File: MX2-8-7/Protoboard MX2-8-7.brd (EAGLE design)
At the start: 64.6 x 71.2 mm, 442 parts, among them J1 DCJ0202

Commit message: Gerb files
Added herb files
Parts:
- moved PAD442 1.27 mm to (55.9, 7.62)
- moved PAD443 1.27 mm to (40.6, 7.62)
- moved PAD444 1.27 mm to (5.08, 7.62)
- moved PAD445 1.27 mm to (53.3, 7.62)
- moved PAD446 1.27 mm to (38.1, 7.62)
- moved PAD447 1.27 mm to (7.62, 7.62)
- moved PAD448 1.27 mm to (50.8, 7.62)
- moved PAD449 1.27 mm to (35.6, 7.62)
- moved PAD450 1.27 mm to (10.2, 7.62)
- moved PAD451 1.27 mm to (48.3, 7.62)
- moved PAD452 1.27 mm to (33.0, 7.62)
- moved PAD453 1.27 mm to (12.7, 7.62)
- moved PAD454 1.27 mm to (45.7, 7.62)
- moved PAD455 1.27 mm to (30.5, 7.62)
- moved PAD456 1.27 mm to (15.2, 7.62)
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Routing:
- net VDD: track 181.4 -> 187.0 mm
- net N$7: track 20.5 -> 22.9 mm
- net N$33: track 20.4 -> 22.8 mm
- net N$30: track 20.4 -> 22.8 mm
- net N$26: track 20.4 -> 22.6 mm
- net N$5: track 20.4 -> 22.6 mm
- net N$29: track 20.6 -> 22.7 mm
- net N$16: track 20.5 -> 22.6 mm
- net N$10: track 20.7 -> 22.7 mm
- net N$20: track 20.3 -> 22.3 mm
- net N$22: track 21.1 -> 22.9 mm
- net N$40: track 21.0 -> 22.7 mm
- net N$37: track 20.4 -> 22.1 mm
- net N$13: track 20.4 -> 22.1 mm
- net N$19: track 21.1 -> 22.7 mm
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- added copper zone on layer 16, net GND

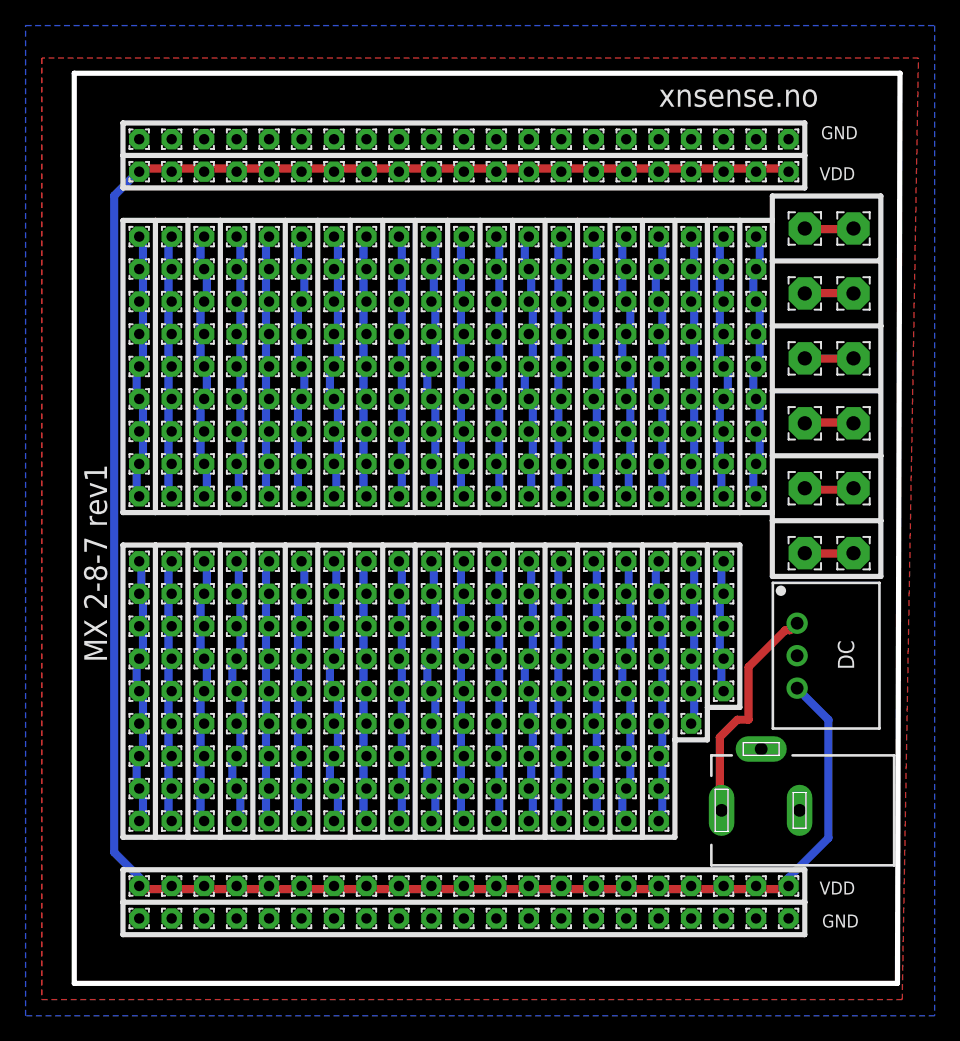
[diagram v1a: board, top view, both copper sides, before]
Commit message: Adjusted Polygon
Adjusted Polygon on all boxes. Changed length on MX-4-7-6 to fit the
box, it was 2mm to long.
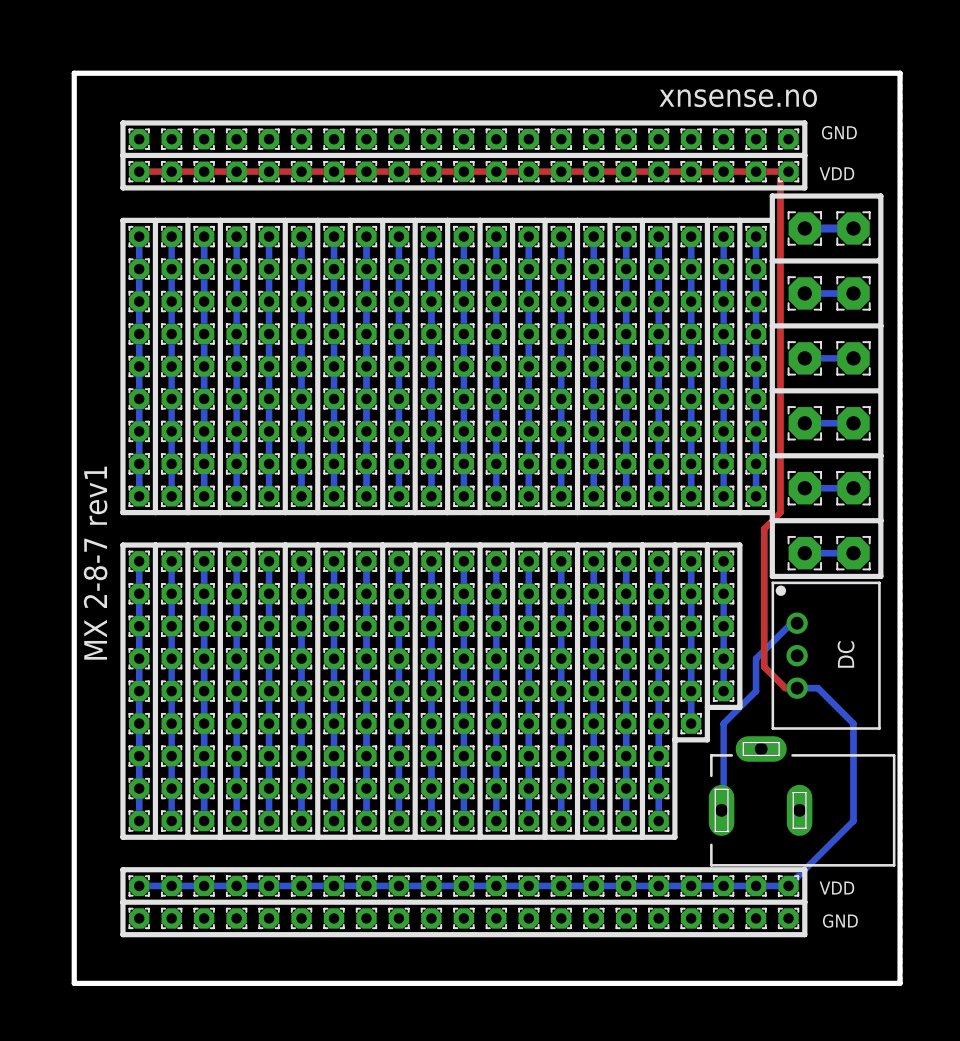
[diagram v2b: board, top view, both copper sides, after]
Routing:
- net VDD: track 187.0 -> 164.8 mm
- net N$15: track 23.0 -> 20.3 mm
- net N$22: track 22.9 -> 20.3 mm
- net N$6: track 22.9 -> 20.3 mm
- net N$7: track 22.9 -> 20.3 mm
- net N$39: track 22.8 -> 20.3 mm
- net N$3: track 22.8 -> 20.3 mm
- net N$33: track 22.8 -> 20.3 mm
- net N$30: track 22.8 -> 20.3 mm
- net N$40: track 22.7 -> 20.3 mm
- net N$29: track 22.7 -> 20.3 mm
- net N$19: track 22.7 -> 20.3 mm
- net N$10: track 22.7 -> 20.3 mm
- net N$12: track 22.7 -> 20.3 mm
- net N$5: track 22.6 -> 20.3 mm
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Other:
- outline, holes or cut-outs redrawn

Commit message: Update to rev2
Updated to Pin headers instead of single wire pads
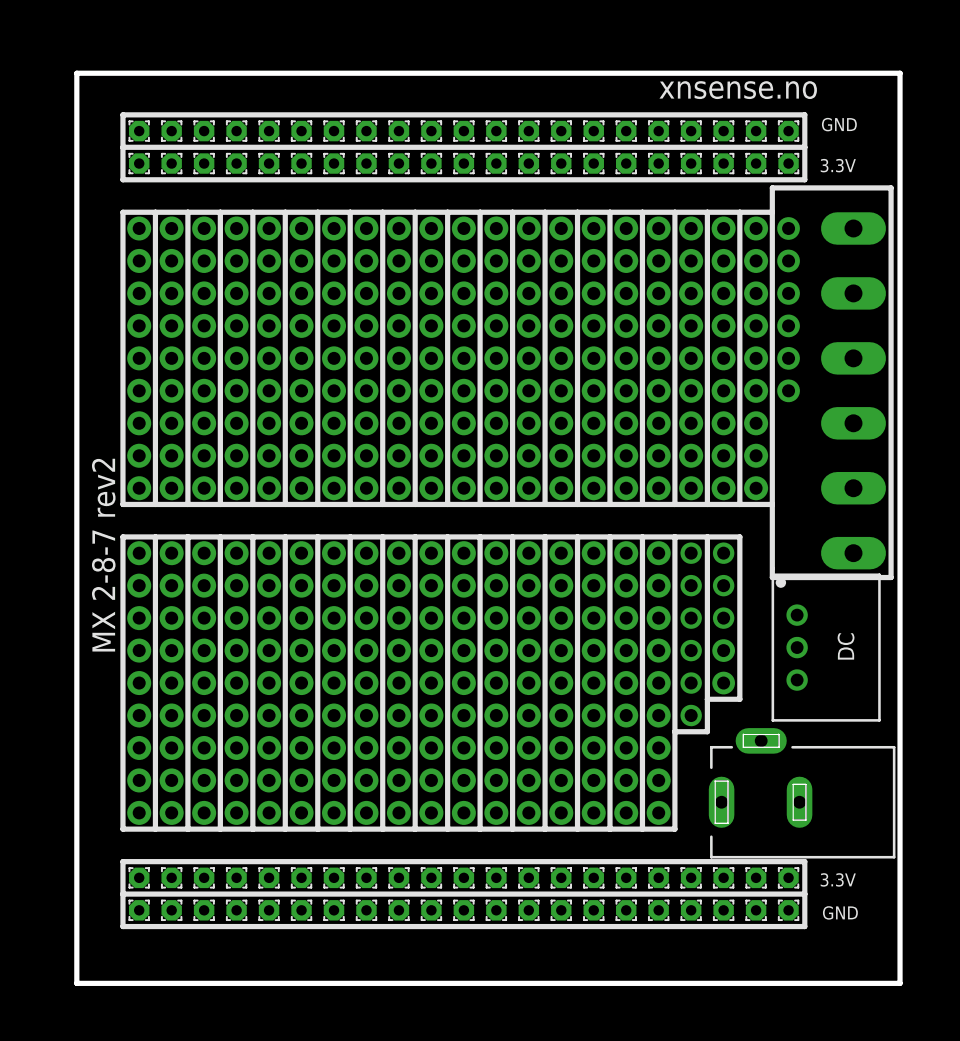
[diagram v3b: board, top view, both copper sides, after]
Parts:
- removed PAD100, PAD101, PAD102, PAD103, PAD104, PAD105, PAD106, PAD107, PAD108, PAD109, PAD110, PAD111, PAD112, PAD113, PAD114, PAD115, PAD116, PAD117, PAD118, PAD119, PAD120, PAD121, PAD122, PAD123, PAD124, PAD125, PAD126, PAD127, PAD128, PAD129, PAD130, PAD131, PAD132, PAD133, PAD134, PAD135, PAD136, PAD137, PAD138, PAD139, PAD140, PAD141, PAD142, PAD143, PAD144, PAD145, PAD146, PAD147, PAD148, PAD149, PAD150, PAD151, PAD152, PAD153, PAD154, PAD155, PAD156, PAD157, PAD158, PAD159, PAD160, PAD161, PAD162, PAD163, PAD164, PAD165, PAD166, PAD167, PAD168, PAD169, PAD170, PAD171, PAD172, PAD173, PAD174, PAD175, PAD176, PAD177, PAD178, PAD179, PAD180, PAD181, PAD182, PAD183, PAD184, PAD185, PAD186, PAD187, PAD188, PAD189, PAD190, PAD191, PAD192, PAD193, PAD194, PAD195, PAD196, PAD197, PAD198, PAD199, PAD20, PAD200, PAD201, PAD202, PAD203, PAD204, PAD205, PAD206, PAD207, PAD208, PAD209, PAD21, PAD210, PAD211, PAD212, PAD213, PAD214, PAD215, PAD216, PAD217, PAD218, PAD219, PAD220, PAD221, PAD222, PAD223, PAD224, PAD225, PAD226, PAD227, PAD228, PAD229, PAD230, PAD231, PAD232, PAD233, PAD234, PAD235, PAD236, PAD237, PAD238, PAD239, PAD240, PAD241, PAD242, PAD243, PAD244, PAD245, PAD246, PAD247, PAD248, PAD249, PAD250, PAD251, PAD252, PAD253, PAD254, PAD255, PAD256, PAD257, PAD258, PAD259, PAD260, PAD261, PAD262, PAD263, PAD264, PAD265, PAD266, PAD267, PAD268, PAD269, PAD270, PAD271, PAD272, PAD273, PAD274, PAD275, PAD276, PAD277, PAD278, PAD279, PAD280, PAD281, PAD282, PAD283, PAD284, PAD285, PAD286, PAD287, PAD288, PAD289, PAD290, PAD291, PAD292, PAD293, PAD294, PAD295, PAD296, PAD297, PAD298, PAD299, PAD300, PAD301, PAD302, PAD303, PAD304, PAD305, PAD306, PAD307, PAD308, PAD309, PAD310, PAD311, PAD312, PAD313, PAD314, PAD315, PAD316, PAD317, PAD318, PAD319, PAD320, PAD321, PAD331, PAD332, PAD333, PAD334, PAD335, PAD336, PAD337, PAD338, PAD339, PAD340, PAD341, PAD342, PAD343, PAD344, PAD345, PAD346, PAD347, PAD348, PAD349, PAD350, PAD351, PAD352, PAD353, PAD354, PAD355, PAD356, PAD357, PAD358, PAD359, PAD360, PAD361, PAD362, PAD363, PAD364, PAD365, PAD366, PAD367, PAD368, PAD369, PAD370, PAD371, PAD372, PAD373, PAD374, PAD375, PAD376, PAD377, PAD378, PAD379, PAD38, PAD380, PAD381, PAD382, PAD383, PAD384, PAD385, PAD386, PAD387, PAD388, PAD389, PAD390, PAD391, PAD392, PAD393, PAD394, PAD395, PAD42, PAD47, PAD48, PAD49, PAD50, PAD51, PAD52, PAD53, PAD54, PAD55, PAD56, PAD57, PAD58, PAD59, PAD60, PAD61, PAD62, PAD63, PAD64, PAD65, PAD66, PAD67, PAD68, PAD69, PAD70, PAD71, PAD72, PAD73, PAD74, PAD75, PAD76, PAD77, PAD78, PAD79, PAD80, PAD81, PAD82, PAD83, PAD84, PAD85, PAD86, PAD87, PAD88, PAD89, PAD90, PAD91, PAD92, PAD93, PAD94, PAD95, PAD96, PAD97, PAD98, PAD99: (no value), wirepad:1,6/0,8
- removed PAD322, PAD323, PAD324, PAD325, PAD326, PAD327, PAD328, PAD329, PAD397, PAD398, PAD399, PAD400: (no value), wirepad:2,54/1,1
- added J10, J11, J12, J13, J14, J15, J16, J17, J18, J19, J2, J20, J21, J22, J23, J24, J25, J26, J27, J28, J29, J3, J30, J31, J32, J33, J34, J35, J36, J37, J38, J4, J5, J6, J7, J8, J9: (no value), SparkFun-Connectors:1X09_NO_SILK
- added JP1, JP10, JP11, JP3, JP4, JP7, JP8, JP9: (no value), adafruit:1X01-CLEANBIG
- added JP12, JP13, JP14, JP15, JP16, JP17: (no value), adafruit:1X1-BIGPOGO
- added JP2, JP5, JP6: (no value), adafruit:1X03-CLEANBIG
- moved PAD15 0.64 mm to (55.9, 64.1)
- moved PAD25 0.64 mm to (5.08, 64.1)
- moved PAD26 0.64 mm to (7.62, 64.1)
- moved PAD27 0.64 mm to (30.5, 64.1)
- moved PAD28 0.64 mm to (25.4, 64.1)
- moved PAD29 0.64 mm to (27.9, 64.1)
- moved PAD30 0.64 mm to (15.2, 64.1)
- moved PAD31 0.64 mm to (12.7, 64.1)
- moved PAD32 0.64 mm to (10.2, 64.1)
- moved PAD33 0.64 mm to (17.8, 64.1)
- moved PAD34 0.64 mm to (33.0, 64.1)
- moved PAD35 0.64 mm to (35.6, 64.1)
- moved PAD36 0.64 mm to (20.3, 64.1)
- moved PAD37 0.64 mm to (43.2, 64.1)
- moved PAD39 0.64 mm to (22.9, 64.1)
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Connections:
- net N$1: now also J2.1, J2.2, J2.3, J2.4, J2.5, J2.6, J2.7, J2.8, J2.9; no longer PAD391.1, PAD392.1, PAD393.1, PAD394.1, PAD395.1
- net N$10: now also J10.1, J10.2, J10.3, J10.4, J10.5, J10.6, J10.7, J10.8, J10.9; no longer PAD106.1, PAD107.1, PAD108.1, PAD109.1, PAD110.1, PAD111.1, PAD112.1, PAD113.1, PAD114.1
- net N$11: now also J11.1, J11.2, J11.3, J11.4, J11.5, J11.6, J11.7, J11.8, J11.9; no longer PAD115.1, PAD116.1, PAD117.1, PAD118.1, PAD119.1, PAD120.1, PAD121.1, PAD122.1, PAD123.1
- net N$12: now also J12.1, J12.2, J12.3, J12.4, J12.5, J12.6, J12.7, J12.8, J12.9; no longer PAD124.1, PAD125.1, PAD126.1, PAD127.1, PAD128.1, PAD129.1, PAD130.1, PAD131.1, PAD132.1
- net N$13: now also J13.1, J13.2, J13.3, J13.4, J13.5, J13.6, J13.7, J13.8, J13.9; no longer PAD133.1, PAD134.1, PAD135.1, PAD136.1, PAD137.1, PAD138.1, PAD139.1, PAD140.1, PAD141.1
- net N$14: now also J14.1, J14.2, J14.3, J14.4, J14.5, J14.6, J14.7, J14.8, J14.9; no longer PAD142.1, PAD143.1, PAD144.1, PAD145.1, PAD146.1, PAD147.1, PAD148.1, PAD149.1, PAD150.1
- net N$15: now also J15.1, J15.2, J15.3, J15.4, J15.5, J15.6, J15.7, J15.8, J15.9; no longer PAD151.1, PAD152.1, PAD153.1, PAD154.1, PAD155.1, PAD156.1, PAD157.1, PAD158.1, PAD159.1
- net N$16: now also J16.1, J16.2, J16.3, J16.4, J16.5, J16.6, J16.7, J16.8, J16.9; no longer PAD160.1, PAD161.1, PAD162.1, PAD163.1, PAD164.1, PAD165.1, PAD166.1, PAD167.1, PAD168.1
- net N$17: now also J17.1, J17.2, J17.3, J17.4, J17.5, J17.6, J17.7, J17.8, J17.9; no longer PAD169.1, PAD170.1, PAD171.1, PAD172.1, PAD173.1, PAD174.1, PAD175.1, PAD176.1, PAD177.1
- net N$18: now also J18.1, J18.2, J18.3, J18.4, J18.5, J18.6, J18.7, J18.8, J18.9; no longer PAD178.1, PAD179.1, PAD180.1, PAD181.1, PAD182.1, PAD183.1, PAD184.1, PAD185.1, PAD186.1
- net N$19: now also J19.1, J19.2, J19.3, J19.4, J19.5, J19.6, J19.7, J19.8, J19.9; no longer PAD187.1, PAD188.1, PAD189.1, PAD190.1, PAD191.1, PAD192.1, PAD193.1, PAD194.1, PAD195.1
- net N$2: now also JP1.1, JP12.P$1; no longer PAD322.1, PAD323.1
- net N$20: now also J20.1, J20.2, J20.3, J20.4, J20.5, J20.6, J20.7, J20.8, J20.9; no longer PAD196.1, PAD197.1, PAD198.1, PAD199.1, PAD200.1, PAD201.1, PAD202.1, PAD203.1, PAD204.1
- net N$21: now also J21.1, J21.2, J21.3, J21.4, J21.5, J21.6, J21.7, J21.8, J21.9; no longer PAD205.1, PAD206.1, PAD207.1, PAD208.1, PAD209.1, PAD210.1, PAD211.1, PAD212.1, PAD213.1
- net N$22: now also J22.1, J22.2, J22.3, J22.4, J22.5, J22.6, J22.7, J22.8, J22.9; no longer PAD214.1, PAD215.1, PAD216.1, PAD217.1, PAD218.1, PAD219.1, PAD220.1, PAD221.1, PAD222.1
- net N$23: now also J23.1, J23.2, J23.3, J23.4, J23.5, J23.6, J23.7, J23.8, J23.9; no longer PAD223.1, PAD224.1, PAD225.1, PAD226.1, PAD227.1, PAD228.1, PAD229.1, PAD230.1, PAD231.1
- net N$24: now also J24.1, J24.2, J24.3, J24.4, J24.5, J24.6, J24.7, J24.8, J24.9; no longer PAD232.1, PAD233.1, PAD234.1, PAD235.1, PAD236.1, PAD237.1, PAD238.1, PAD239.1, PAD240.1
- net N$25: now also J25.1, J25.2, J25.3, J25.4, J25.5, J25.6, J25.7, J25.8, J25.9; no longer PAD241.1, PAD242.1, PAD243.1, PAD244.1, PAD245.1, PAD246.1, PAD247.1, PAD248.1, PAD249.1
- net N$26: now also J26.1, J26.2, J26.3, J26.4, J26.5, J26.6, J26.7, J26.8, J26.9; no longer PAD250.1, PAD251.1, PAD252.1, PAD253.1, PAD254.1, PAD255.1, PAD256.1, PAD257.1, PAD258.1
- net N$27: now also J27.1, J27.2, J27.3, J27.4, J27.5, J27.6, J27.7, J27.8, J27.9; no longer PAD259.1, PAD260.1, PAD261.1, PAD262.1, PAD263.1, PAD264.1, PAD265.1, PAD266.1, PAD267.1
- net N$28: now also J28.1, J28.2, J28.3, J28.4, J28.5, J28.6, J28.7, J28.8, J28.9; no longer PAD268.1, PAD269.1, PAD270.1, PAD271.1, PAD272.1, PAD273.1, PAD274.1, PAD275.1, PAD276.1
- net N$29: now also J29.1, J29.2, J29.3, J29.4, J29.5, J29.6, J29.7, J29.8, J29.9; no longer PAD277.1, PAD278.1, PAD279.1, PAD280.1, PAD281.1, PAD282.1, PAD283.1, PAD284.1, PAD285.1
- net N$3: now also J3.1, J3.2, J3.3, J3.4, J3.5, J3.6, J3.7, J3.8, J3.9; no longer PAD20.1, PAD21.1, PAD38.1, PAD42.1, PAD47.1, PAD48.1, PAD49.1, PAD50.1, PAD51.1
- net N$30: now also J30.1, J30.2, J30.3, J30.4, J30.5, J30.6, J30.7, J30.8, J30.9; no longer PAD286.1, PAD287.1, PAD288.1, PAD289.1, PAD290.1, PAD291.1, PAD292.1, PAD293.1, PAD294.1
- net N$31: now also J31.1, J31.2, J31.3, J31.4, J31.5, J31.6, J31.7, J31.8, J31.9; no longer PAD295.1, PAD296.1, PAD297.1, PAD298.1, PAD299.1, PAD300.1, PAD301.1, PAD302.1, PAD303.1
- net N$32: now also J32.1, J32.2, J32.3, J32.4, J32.5, J32.6, J32.7, J32.8, J32.9; no longer PAD304.1, PAD305.1, PAD306.1, PAD307.1, PAD308.1, PAD309.1, PAD310.1, PAD311.1, PAD312.1
- net N$33: now also J33.1, J33.2, J33.3, J33.4, J33.5, J33.6, J33.7, J33.8, J33.9; no longer PAD313.1, PAD314.1, PAD315.1, PAD316.1, PAD317.1, PAD318.1, PAD319.1, PAD320.1, PAD321.1
- net N$34: now also JP13.P$1, JP7.1; no longer PAD324.1, PAD325.1
- net N$35: now also J34.1, J34.2, J34.3, J34.4, J34.5, J34.6, J34.7, J34.8, J34.9; no longer PAD331.1, PAD332.1, PAD333.1, PAD334.1, PAD335.1, PAD336.1, PAD337.1, PAD338.1, PAD339.1
- net N$36: now also J35.1, J35.2, J35.3, J35.4, J35.5, J35.6, J35.7, J35.8, J35.9; no longer PAD340.1, PAD341.1, PAD342.1, PAD343.1, PAD344.1, PAD345.1, PAD346.1, PAD347.1, PAD348.1
- net N$37: now also J36.1, J36.2, J36.3, J36.4, J36.5, J36.6, J36.7, J36.8, J36.9; no longer PAD349.1, PAD350.1, PAD351.1, PAD352.1, PAD353.1, PAD354.1, PAD355.1, PAD356.1, PAD357.1
- net N$38: now also J37.1, J37.2, J37.3, J37.4, J37.5, J37.6, J37.7, J37.8, J37.9; no longer PAD358.1, PAD359.1, PAD360.1, PAD361.1, PAD362.1, PAD363.1, PAD364.1, PAD365.1, PAD366.1
- net N$39: now also J38.1, J38.2, J38.3, J38.4, J38.5, J38.6, J38.7, J38.8, J38.9; no longer PAD367.1, PAD368.1, PAD369.1, PAD370.1, PAD371.1, PAD372.1, PAD373.1, PAD374.1, PAD375.1
- net N$4: now also J4.1, J4.2, J4.3, J4.4, J4.5, J4.6, J4.7, J4.8, J4.9; no longer PAD52.1, PAD53.1, PAD54.1, PAD55.1, PAD56.1, PAD57.1, PAD58.1, PAD59.1, PAD60.1
- net N$40: now also JP5.1, JP5.2, JP5.3, JP6.1, JP6.2, JP6.3; no longer PAD376.1, PAD377.1, PAD378.1, PAD379.1, PAD380.1, PAD381.1, PAD382.1, PAD383.1, PAD384.1
- net N$41: now also JP2.1, JP2.2, JP2.3, JP3.1, JP4.1; no longer PAD385.1, PAD386.1, PAD387.1, PAD388.1, PAD389.1, PAD390.1
- net N$42: now also JP14.P$1, JP8.1; no longer PAD326.1, PAD327.1
- net N$43: now also JP15.P$1, JP9.1; no longer PAD328.1, PAD329.1
- net N$44: now also JP10.1, JP16.P$1; no longer PAD399.1, PAD400.1
- net N$45: now also JP11.1, JP17.P$1; no longer PAD397.1, PAD398.1
- net N$5: now also J5.1, J5.2, J5.3, J5.4, J5.5, J5.6, J5.7, J5.8, J5.9; no longer PAD61.1, PAD62.1, PAD63.1, PAD64.1, PAD65.1, PAD66.1, PAD67.1, PAD68.1, PAD69.1
- net N$6: now also J6.1, J6.2, J6.3, J6.4, J6.5, J6.6, J6.7, J6.8, J6.9; no longer PAD70.1, PAD71.1, PAD72.1, PAD73.1, PAD74.1, PAD75.1, PAD76.1, PAD77.1, PAD78.1
- net N$7: now also J7.1, J7.2, J7.3, J7.4, J7.5, J7.6, J7.7, J7.8, J7.9; no longer PAD79.1, PAD80.1, PAD81.1, PAD82.1, PAD83.1, PAD84.1, PAD85.1, PAD86.1, PAD87.1
- net N$8: now also J8.1, J8.2, J8.3, J8.4, J8.5, J8.6, J8.7, J8.8, J8.9; no longer PAD88.1, PAD89.1, PAD90.1, PAD91.1, PAD92.1, PAD93.1, PAD94.1, PAD95.1, PAD96.1
- net N$9: now also J9.1, J9.2, J9.3, J9.4, J9.5, J9.6, J9.7, J9.8, J9.9; no longer PAD100.1, PAD101.1, PAD102.1, PAD103.1, PAD104.1, PAD105.1, PAD97.1, PAD98.1, PAD99.1
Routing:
- net VDD: track 164.8 -> 0.00 mm
- net N$39: track 20.3 -> 0.00 mm
- net N$37: track 20.3 -> 0.00 mm
- net N$35: track 20.3 -> 0.00 mm
- net N$33: track 20.3 -> 0.00 mm
- net N$31: track 20.3 -> 0.00 mm
- net N$29: track 20.3 -> 0.00 mm
- net N$27: track 20.3 -> 0.00 mm
- net N$24: track 20.3 -> 0.00 mm
- net N$9: track 20.3 -> 0.00 mm
- net N$8: track 20.3 -> 0.00 mm
- net N$7: track 20.3 -> 0.00 mm
- net N$6: track 20.3 -> 0.00 mm
- net N$5: track 20.3 -> 0.00 mm
- net N$40: track 20.3 -> 0.00 mm
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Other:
- board size 64.6 x 71.2 mm -> 64.4 x 71.2 mm
- board text added: "3.3V"
- board text added: "MX 2-8-7 rev2"
- board text removed: "MX 2-8-7 rev1"
- board text removed: "VDD"

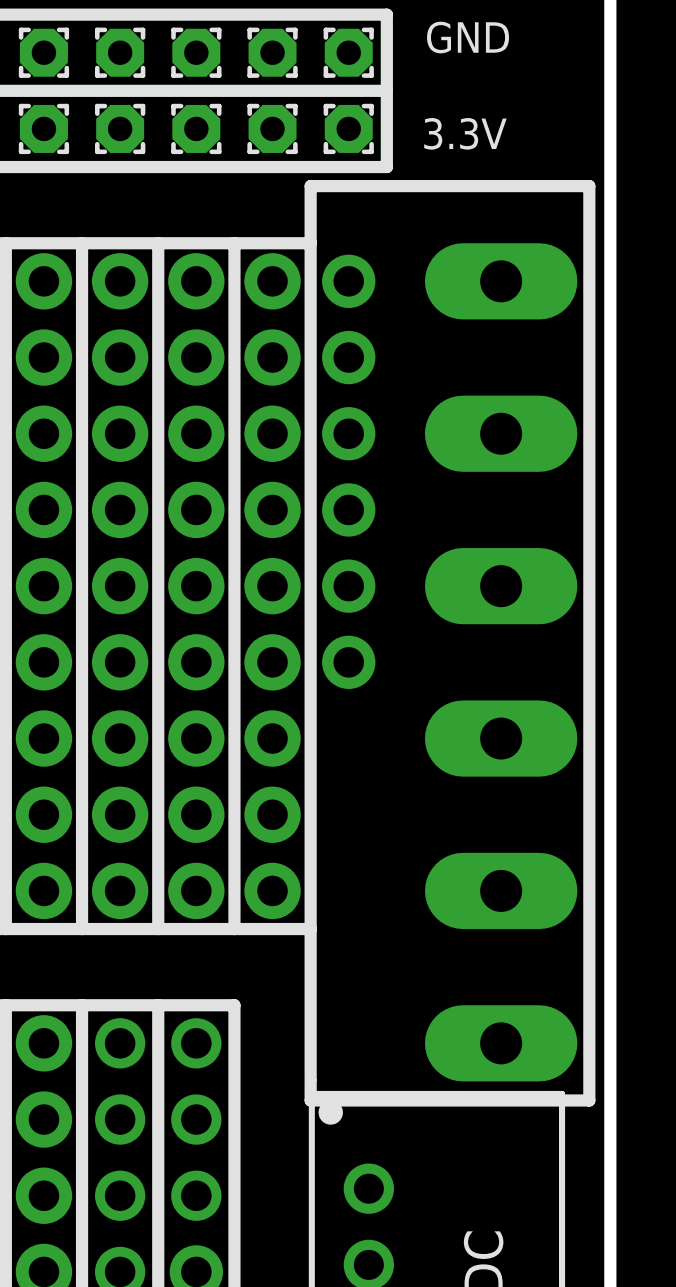
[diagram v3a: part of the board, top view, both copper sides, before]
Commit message: Change usb connector
Change to correct usb connecter and moved esp8266 bit more onto the
board.
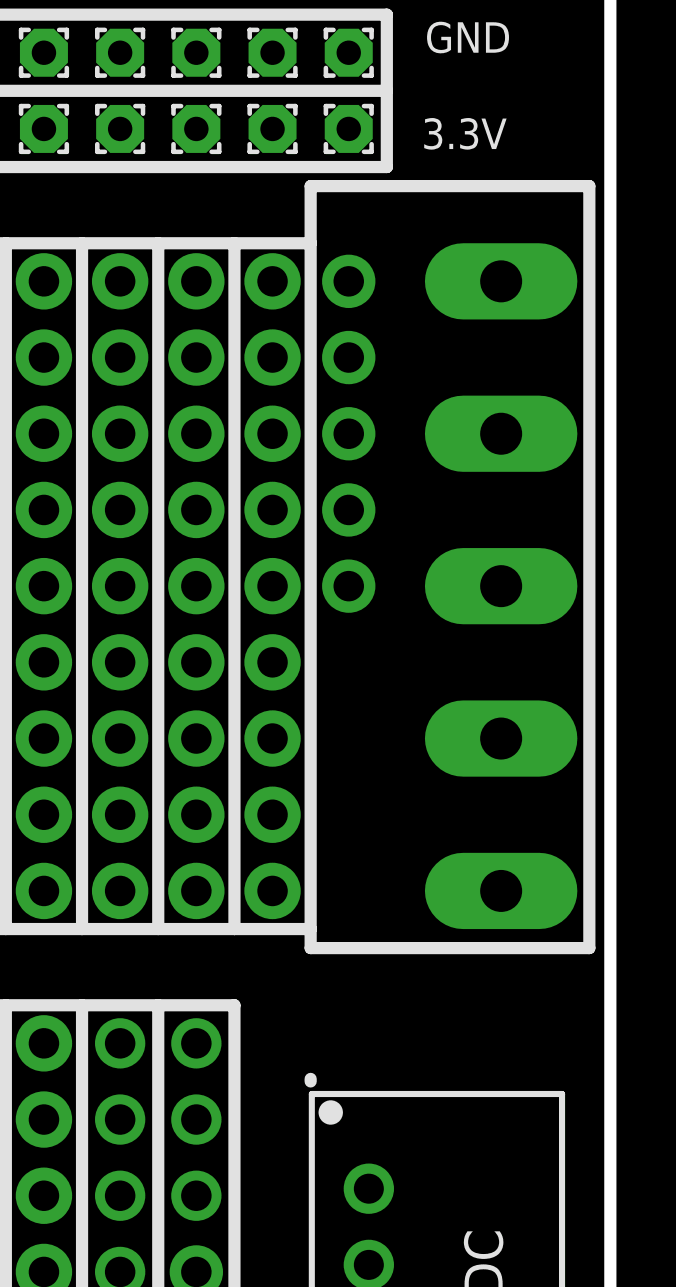
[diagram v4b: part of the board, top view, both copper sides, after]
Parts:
- removed JP11: (no value), adafruit:1X01-CLEANBIG
- removed JP17: (no value), adafruit:1X1-BIGPOGO
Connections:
- removed net N$45: JP11.1, JP17.P$1
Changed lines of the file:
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@@
 <wire x1="63.9" y1="62.23" x2="54.61" y2="62.23" width="0.4064" layer="25"/>
 <wire x1="54.61" y1="62.23" x2="54.61" y2="60.325" width="0.4064" layer="25"/>
-<wire x1="63.9" y1="62.23" x2="63.9" y2="31.75" width="0.4064" layer="25"/>
-<wire x1="54.61" y1="32.47" x2="54.61" y2="37.465" width="0.4064" layer="25"/>
+<wire x1="63.9" y1="62.23" x2="63.9" y2="36.83" width="0.4064" layer="25"/>
 <text x="58.42" y="66.675" size="1.016" layer="25">GND</text>
 <text x="58.5" y="5.005" size="1.016" layer="25">GND</text>
@@
 <dimension x1="3.81" y1="4.445" x2="3.81" y2="0" x3="-3.81" y3="2.2225" textsize="1.778" layer="47"/>
 <dimension x1="54.61" y1="62.23" x2="54.61" y2="71.2" x3="69.85" y3="66.715" textsize="1.778" layer="47"/>
+<wire x1="54.61" y1="36.83" x2="54.61" y2="37.465" width="0.4064" layer="25"/>
 <wire x1="52.07" y1="37.465" x2="54.61" y2="37.465" width="0.4064" layer="25"/>
 <wire x1="52.07" y1="60.325" x2="54.61" y2="60.325" width="0.4064" layer="25"/>
 <dimension x1="0" y1="0" x2="0" y2="71.2" x3="-8.89" y3="35.6" textsize="1.778" layer="44"/>
 <dimension x1="0.2" y1="71.2" x2="64.6" y2="71.2" x3="32.4" y3="76.2" textsize="1.778" layer="44"/>
-<wire x1="54.61" y1="32.385" x2="54.61" y2="31.75" width="0.4064" layer="25"/>
-<wire x1="54.61" y1="31.75" x2="63.9" y2="31.75" width="0.4064" layer="25"/>
+<wire x1="54.61" y1="32.385" x2="54.61" y2="32.47" width="0.4064" layer="25"/>
+<wire x1="54.61" y1="36.83" x2="63.9" y2="36.83" width="0.4064" layer="25"/>
 <dimension x1="64.6" y1="71.2" x2="66.8" y2="71.2" x3="65.7" y3="30.48" textsize="1.778" layer="47"/>
 <dimension x1="60.96" y1="59.055" x2="64.6" y2="59.055" x3="62.78" y3="59.055" textsize="1.778" layer="47"/>
@@
 <attribute name="VALUE" x="54.61" y="45.72" size="1.27" layer="27"/>
 </element>
-<element name="JP11" library="adafruit" package="1X01-CLEANBIG" value="" x="55.88" y="46.355" smashed="yes">
-<attribute name="VALUE" x="54.61" y="43.18" size="1.27" layer="27"/>
-</element>
 <element name="JP12" library="adafruit" package="1X1-BIGPOGO" value="" x="60.96" y="59.055"/>
 <element name="JP13" library="adafruit" package="1X1-BIGPOGO" value="" x="60.96" y="53.975"/>
@@
 <element name="JP15" library="adafruit" package="1X1-BIGPOGO" value="" x="60.96" y="43.815"/>
 <element name="JP16" library="adafruit" package="1X1-BIGPOGO" value="" x="60.96" y="38.735"/>
-<element name="JP17" library="adafruit" package="1X1-BIGPOGO" value="" x="60.96" y="33.655"/>
 </elements>
 <signals>
@@
 <wire x1="60.96" y1="38.735" x2="55.88" y2="48.895" width="0" layer="19" extent="1-1"/>
 </signal>
-<signal name="N$45">
-<contactref element="JP17" pad="P$1"/>
-<contactref element="JP11" pad="1"/>
-<wire x1="55.88" y1="46.355" x2="60.96" y2="33.655" width="0" layer="19" extent="1-1"/>
-</signal>
 </signals>

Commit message: Update esp component and usb
test
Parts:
- removed JP2, JP5, JP6: (no value), adafruit:1X03-CLEANBIG
- removed JP3, JP4: (no value), adafruit:1X01-CLEANBIG
- added J39: (no value), SparkFun-Connectors:1X06_NO_SILK
- added J40: (no value), SparkFun-Connectors:1X05_NO_SILK
- added U1: (no value), SparkFun-PowerIC:SOT23-5
- added X1: (no value), microbuilder:4UCONN_20329_V2
- moved DC 3.70 mm to (58.5, 29.4), turned to 180 degrees
- moved J1 1.42 mm to (54.4, 15.4)
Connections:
- net GND: now also U1.2, X1.BASE@1, X1.BASE@2, X1.GND, X1.SPRT@1, X1.SPRT@2, X1.SPRT@3, X1.SPRT@4
- net N$40: now also J39.1, J39.2, J39.3, J39.4, J39.5, J39.6; no longer JP5.1, JP5.2, JP5.3, JP6.1, JP6.2, JP6.3
- net N$41: now also J40.1, J40.2, J40.3, J40.4, J40.5; no longer JP2.1, JP2.2, JP2.3, JP3.1, JP4.1
- net VCC: now also U1.1, U1.3, X1.VBUS
- net VDD: now also U1.5

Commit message: Routed
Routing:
- net VDD: track 0.00 -> 163.0 mm
- net VCC: track 0.00 -> 35.7 mm
- net N$9: track 0.00 -> 20.3 mm
- net N$8: track 0.00 -> 20.3 mm
- net N$7: track 0.00 -> 20.3 mm
- net N$6: track 0.00 -> 20.3 mm
- net N$5: track 0.00 -> 20.3 mm
- net N$4: track 0.00 -> 20.3 mm
- net N$39: track 0.00 -> 20.3 mm
- net N$38: track 0.00 -> 20.3 mm
- net N$37: track 0.00 -> 20.3 mm
- net N$36: track 0.00 -> 20.3 mm
- net N$35: track 0.00 -> 20.3 mm
- net N$33: track 0.00 -> 20.3 mm
- net N$32: track 0.00 -> 20.3 mm
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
